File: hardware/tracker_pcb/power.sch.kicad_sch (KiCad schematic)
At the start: 25 parts, among them U3 LMR51450SDRRR, U4 TPS2121RUXR, U5 TLV1117LV33DCYR

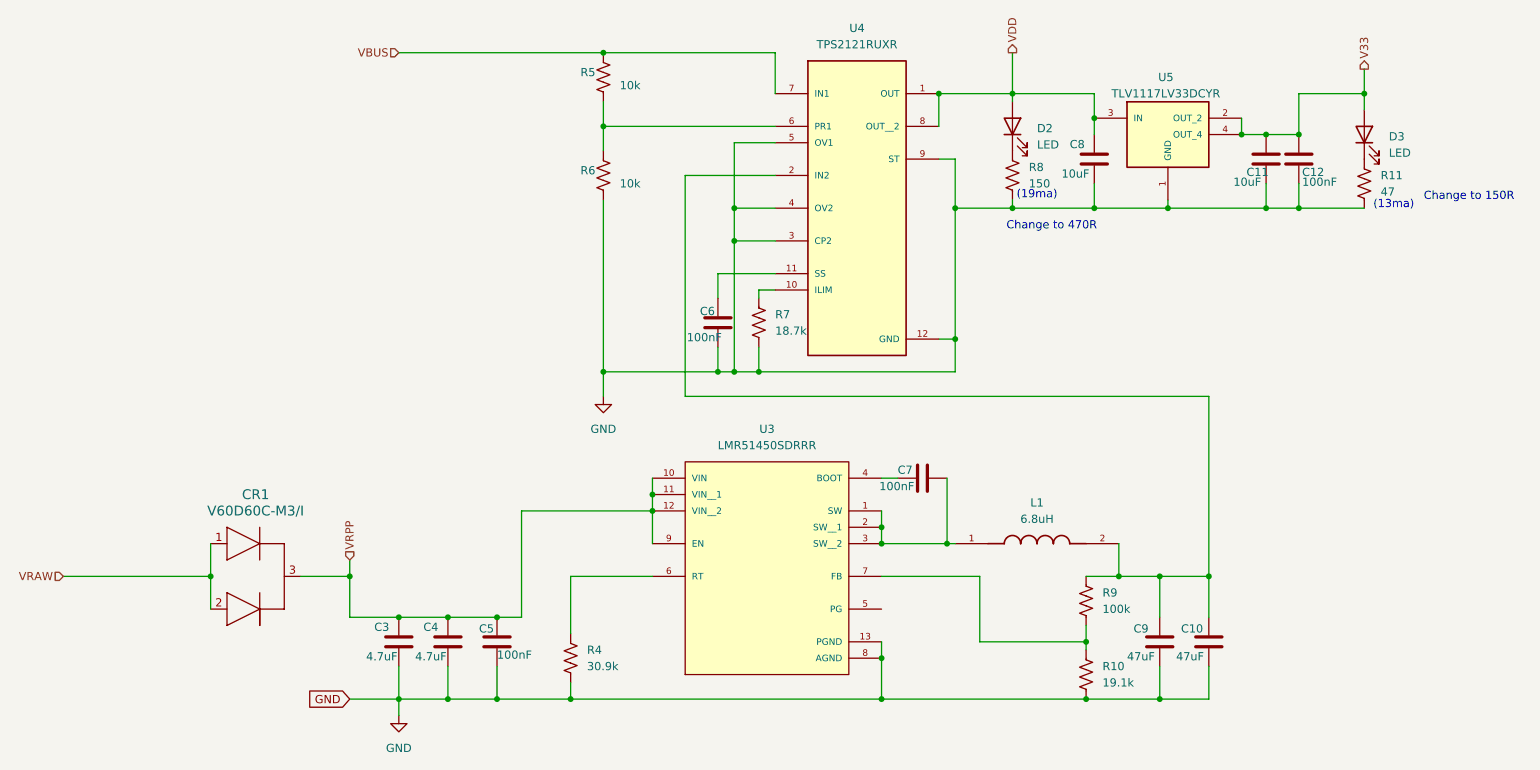
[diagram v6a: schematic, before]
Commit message: more motor safety
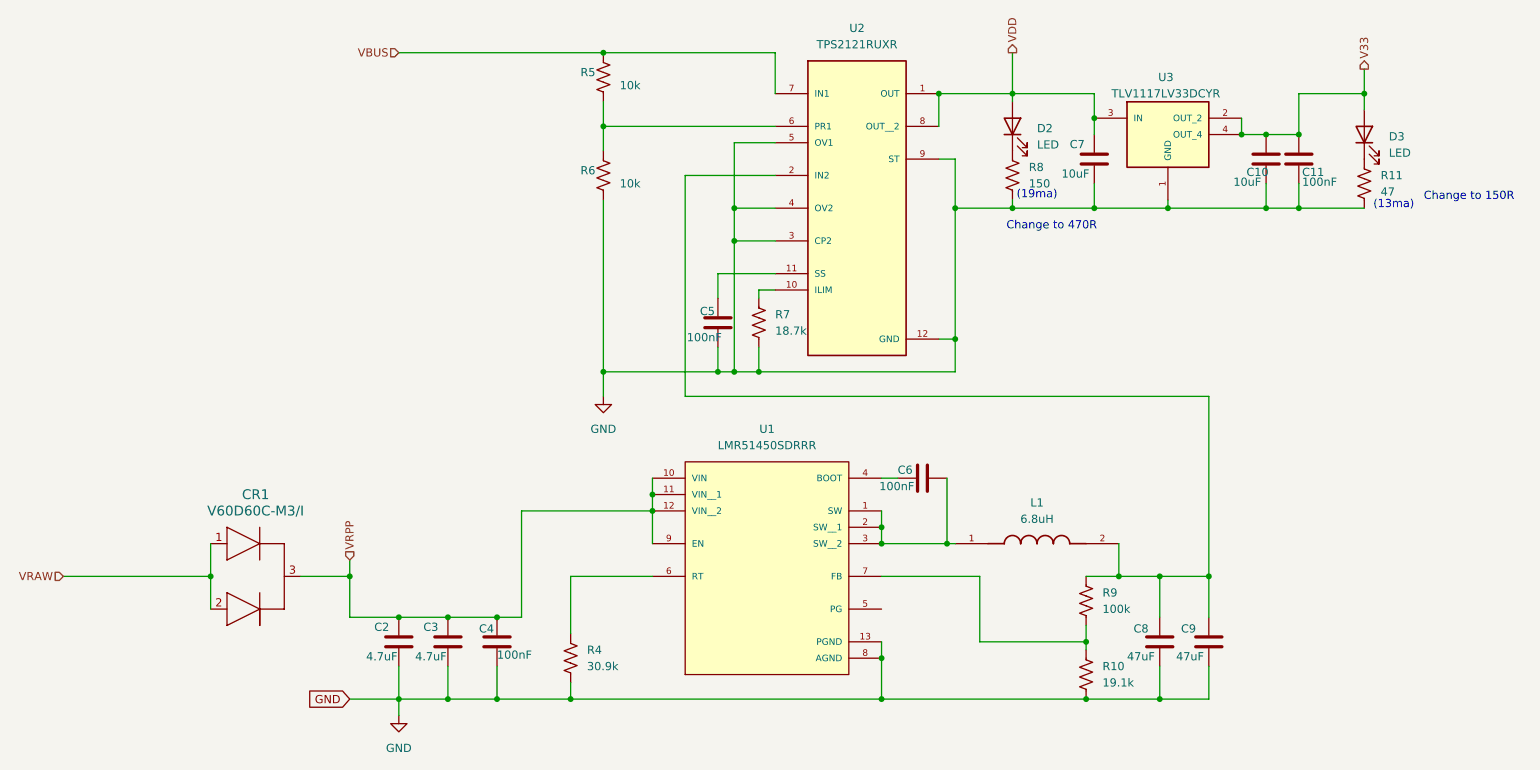
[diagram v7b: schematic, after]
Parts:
- renumbered C11 to C10, C12 to C11, C3 to C2, C4 to C3, C5 to C4, C6 to C5, C7 to C6, C8 to C7, C9 to C8, C10 to C9, U3 to U1, U4 to U2, U5 to U3
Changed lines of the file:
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@@
 		(on_board yes)
 		(dnp no)
-		(property "Reference" "C3"
+		(property "Reference" "C2"
 			(at 92.71 112.014 0)
 			(effects
@@
 			(project "tracker_pcb"
 				(path "/6aaa9514-f94e-4843-90d0-16960e4e49cb/4c324161-c4da-41f3-8af5-33f4b9a0442d"
-					(reference "C3")
+					(reference "C2")
 					(unit 1)
 				)
@@
 		(dnp no)
 		(fields_autoplaced yes)
-		(property "Reference" "U5"
+		(property "Reference" "U3"
 			(at 215.5825 26.67 0)
 			(effects
@@
 			(project ""
 				(path "/6aaa9514-f94e-4843-90d0-16960e4e49cb/4c324161-c4da-41f3-8af5-33f4b9a0442d"
-					(reference "U5")
+					(reference "U3")
 					(unit 1)
 				)
@@
 		(on_board yes)
 		(dnp no)
-		(property "Reference" "C5"
+		(property "Reference" "C4"
 			(at 108.966 112.268 0)
 			(effects
@@
 			(project "tracker_pcb"
 				(path "/6aaa9514-f94e-4843-90d0-16960e4e49cb/4c324161-c4da-41f3-8af5-33f4b9a0442d"
-					(reference "C5")
+					(reference "C4")
 					(unit 1)
 				)
@@
 		(on_board yes)
 		(dnp no)
-		(property "Reference" "C7"
+		(property "Reference" "C6"
 			(at 176.276 87.63 90)
 			(effects
@@
 			(project "tracker_pcb"
 				(path "/6aaa9514-f94e-4843-90d0-16960e4e49cb/4c324161-c4da-41f3-8af5-33f4b9a0442d"
-					(reference "C7")
+					(reference "C6")
 					(unit 1)
 				)
@@
 		(dnp no)
 		(fields_autoplaced yes)
-		(property "Reference" "#PWR013"
+		(property "Reference" "#PWR010"
 			(at 96.52 132.08 0)
 			(effects
@@
 			(project "tracker_pcb"
 				(path "/6aaa9514-f94e-4843-90d0-16960e4e49cb/4c324161-c4da-41f3-8af5-33f4b9a0442d"
-					(reference "#PWR013")
+					(reference "#PWR010")
 					(unit 1)
 				)
@@
 		(on_board yes)
 		(dnp no)
-		(property "Reference" "C11"
+		(property "Reference" "C10"
 			(at 228.092 41.402 0)
 			(effects
@@
 			(project "tracker_pcb"
 				(path "/6aaa9514-f94e-4843-90d0-16960e4e49cb/4c324161-c4da-41f3-8af5-33f4b9a0442d"
-					(reference "C11")
+					(reference "C10")
 					(unit 1)
 				)
@@
 		(on_board yes)
 		(dnp no)
-		(property "Reference" "C4"
+		(property "Reference" "C3"
 			(at 100.33 112.014 0)
 			(effects
@@
 			(project "tracker_pcb"
 				(path "/6aaa9514-f94e-4843-90d0-16960e4e49cb/4c324161-c4da-41f3-8af5-33f4b9a0442d"
-					(reference "C4")
+					(reference "C3")
 					(unit 1)
 				)
@@
 		(dnp no)
 		(fields_autoplaced yes)
-		(property "Reference" "U4"
+		(property "Reference" "U2"
 			(at 167.64 19.05 0)
 			(effects
@@
 			(project ""
 				(path "/6aaa9514-f94e-4843-90d0-16960e4e49cb/4c324161-c4da-41f3-8af5-33f4b9a0442d"
-					(reference "U4")
+					(reference "U2")
 					(unit 1)
 				)
@@
 		(on_board yes)
 		(dnp no)
-		(property "Reference" "C8"
+		(property "Reference" "C7"
 			(at 200.66 37.084 0)
 			(effects
@@
 			(project "tracker_pcb"
 				(path "/6aaa9514-f94e-4843-90d0-16960e4e49cb/4c324161-c4da-41f3-8af5-33f4b9a0442d"
-					(reference "C8")
+					(reference "C7")
 					(unit 1)
 				)
@@
 		(on_board yes)
 		(dnp no)
-		(property "Reference" "C10"
+		(property "Reference" "C9"
 			(at 217.932 112.268 0)
 			(effects
@@
 			(project "tracker_pcb"
 				(path "/6aaa9514-f94e-4843-90d0-16960e4e49cb/4c324161-c4da-41f3-8af5-33f4b9a0442d"
-					(reference "C10")
+					(reference "C9")
 					(unit 1)
 				)
@@
 		(dnp no)
 		(fields_autoplaced yes)
-		(property "Reference" "#PWR014"
+		(property "Reference" "#PWR011"
 			(at 128.27 82.55 0)
 			(effects
@@
 			(project "tracker_pcb"
 				(path "/6aaa9514-f94e-4843-90d0-16960e4e49cb/4c324161-c4da-41f3-8af5-33f4b9a0442d"
-					(reference "#PWR014")
+					(reference "#PWR011")
 					(unit 1)
 				)
@@
 		(on_board yes)
 		(dnp no)
-		(property "Reference" "C9"
+		(property "Reference" "C8"
 			(at 210.566 112.268 0)
 			(effects
@@
 			(project "tracker_pcb"
 				(path "/6aaa9514-f94e-4843-90d0-16960e4e49cb/4c324161-c4da-41f3-8af5-33f4b9a0442d"
-					(reference "C9")
+					(reference "C8")
 					(unit 1)
 				)
@@
 		(dnp no)
 		(fields_autoplaced yes)
-		(property "Reference" "U3"
+		(property "Reference" "U1"
 			(at 153.67 81.28 0)
 			(effects
@@
 			(project ""
 				(path "/6aaa9514-f94e-4843-90d0-16960e4e49cb/4c324161-c4da-41f3-8af5-33f4b9a0442d"
-					(reference "U3")
+					(reference "U1")
 					(unit 1)
 				)
@@
 		(on_board yes)
 		(dnp no)
-		(property "Reference" "C6"
+		(property "Reference" "C5"
 			(at 143.256 62.992 0)
 			(effects
@@
 			(project "tracker_pcb"
 				(path "/6aaa9514-f94e-4843-90d0-16960e4e49cb/4c324161-c4da-41f3-8af5-33f4b9a0442d"
-					(reference "C6")
+					(reference "C5")
 					(unit 1)
 				)
@@
 		(on_board yes)
 		(dnp no)
-		(property "Reference" "C12"
+		(property "Reference" "C11"
 			(at 236.728 41.402 0)
 			(effects
@@
 			(project "tracker_pcb"
 				(path "/6aaa9514-f94e-4843-90d0-16960e4e49cb/4c324161-c4da-41f3-8af5-33f4b9a0442d"
-					(reference "C12")
+					(reference "C11")
 					(unit 1)
 				)
